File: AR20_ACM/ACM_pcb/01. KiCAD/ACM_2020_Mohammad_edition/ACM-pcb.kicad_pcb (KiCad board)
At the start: 2 copper layers, 19.9 x 28 mm, 32 parts, among them J1 TC2030-MCP-NL, P1 Conn_02x15_Odd_Even, Q1 Q_PMOS_DGS, U1 ATmega328P-AU, U2 MCP25625-x-SS, U3 NCV890430MW50TXG, Y1 16.0Mhz

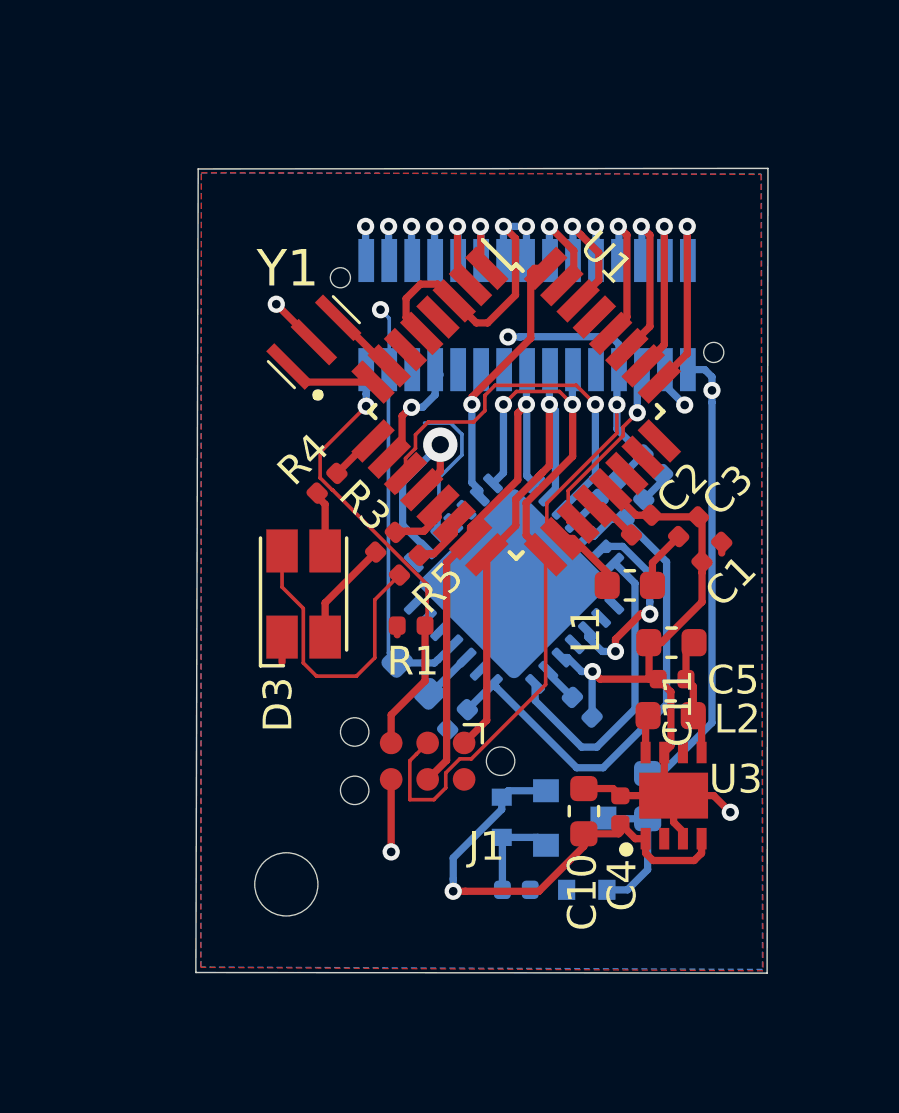
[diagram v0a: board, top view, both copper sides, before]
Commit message: ACM-pcb full connected
ACM -12.01
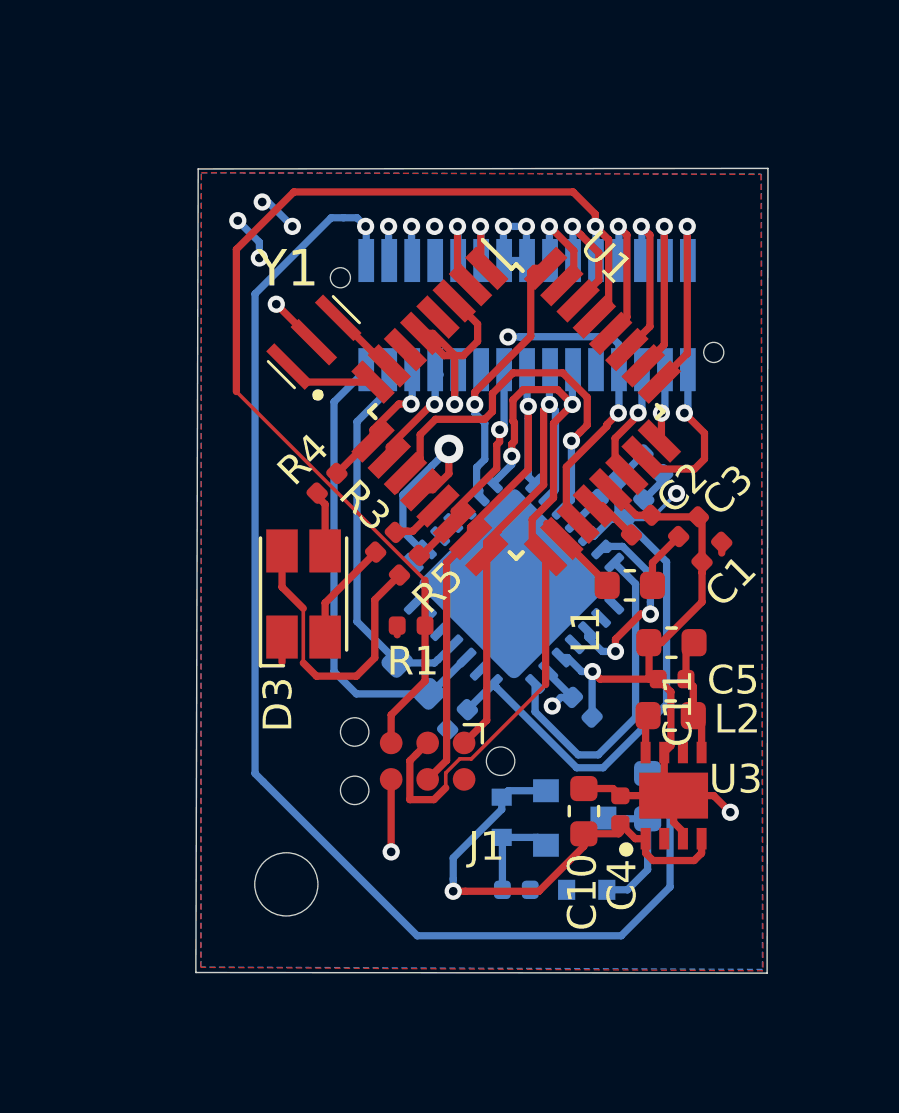
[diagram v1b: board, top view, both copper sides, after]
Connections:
- net /U-Pin19 renamed Net-(P1-Pad19)
- net /U-Pin9 renamed Net-(P1-Pad9)
- P1 pad 1: +12V -> /U-Pin1
- P1 pad 10: /U-Pin10 -> /Reset
- P1 pad 17: /U-Pin17 -> /BLUE_LED
- P1 pad 21: /U-Pin21 -> GND
- P1 pad 24: /U-Pin24 -> GND
- P1 pad 25: /U-Pin25 -> /GREEN_LED
- P1 pad 28: /U-Pin28 -> +5V
- P1 pad 29: /Reset -> /U-Pin29
- P1 pad 30: /U-Pin30 -> +12V
- P1 pad 7: +5V -> /U-Pin7
- R7 pad 2: /U-Pin1 -> /U-Pin29
- U1 pad 19: /U-Pin5 -> /U-Pin7
- U1 pad 22: Net-(U1-Pad22) -> /U-Pin5
- U1 pad 23: /U-Pin7 -> /U-Pin1
- U1 pad 24: Net-(U1-Pad24) -> /U-Pin3
- U2 pad 3: /U-Pin1 -> /U-Pin29
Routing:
- net +12V: track 16.0 -> 44.8 mm
- net /Reset: track 15.7 -> 39.2 mm
- net /U-Pin29: track 0.00 -> 16.5 mm
- net /U-Pin7: track 0.00 -> 11.3 mm, vias 0 -> 2
- net /BLUE_LED: track 1.96 -> 7.77 mm, vias 0 -> 1
- net GND: track 51.4 -> 45.6 mm, vias 6 -> 7
- net +5V: track 43.6 -> 38.6 mm, vias 2 -> 7
- net /U-Pin1: track 1.84 -> 5.93 mm, vias 0 -> 1
- net /GREEN_LED: track 1.81 -> 5.11 mm, vias 0 -> 1
- net /U-Pin5: track 6.72 -> 4.17 mm
- net /U-Pin3: track 1.55 -> 3.14 mm
- net /U-Pin27: track 14.8 -> 13.5 mm, vias 1 -> 0
- net /U-Pin30: track 1.20 -> 0.00 mm, vias 1 -> 0
- net /U-Pin28: track 1.20 -> 0.00 mm, vias 1 -> 0
- net /U-Pin10: track 1.20 -> 0.00 mm, vias 1 -> 0
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
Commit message: final one 12.01
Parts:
- moved C1 14.3 mm to (69.8, 68.3)
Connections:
- net Net-(P1-Pad9) renamed /U-Pin9
- P1 pad 19: Net-(P1-Pad19) -> GND
- P1 pad 24: GND -> +5V
- P1 pad 26: /U-Pin26 -> +5V
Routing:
- net +5V: track 38.6 -> 29.8 mm, vias 7 -> 13
- net /Reset: track 39.2 -> 45.4 mm
- net +12V_Safe: track 17.1 -> 13.6 mm
- net GND: track 45.6 -> 42.6 mm, vias 7 -> 12
- net Net-(D3-Pad2): track 10.4 -> 12.7 mm
- net /U-Pin9: track 0.03 -> 1.25 mm, vias 0 -> 1
- net /U-Pin26: track 1.20 -> 0.00 mm, vias 1 -> 0
- net +12V: track 44.8 -> 45.8 mm
- net (no net): vias 1 -> 0

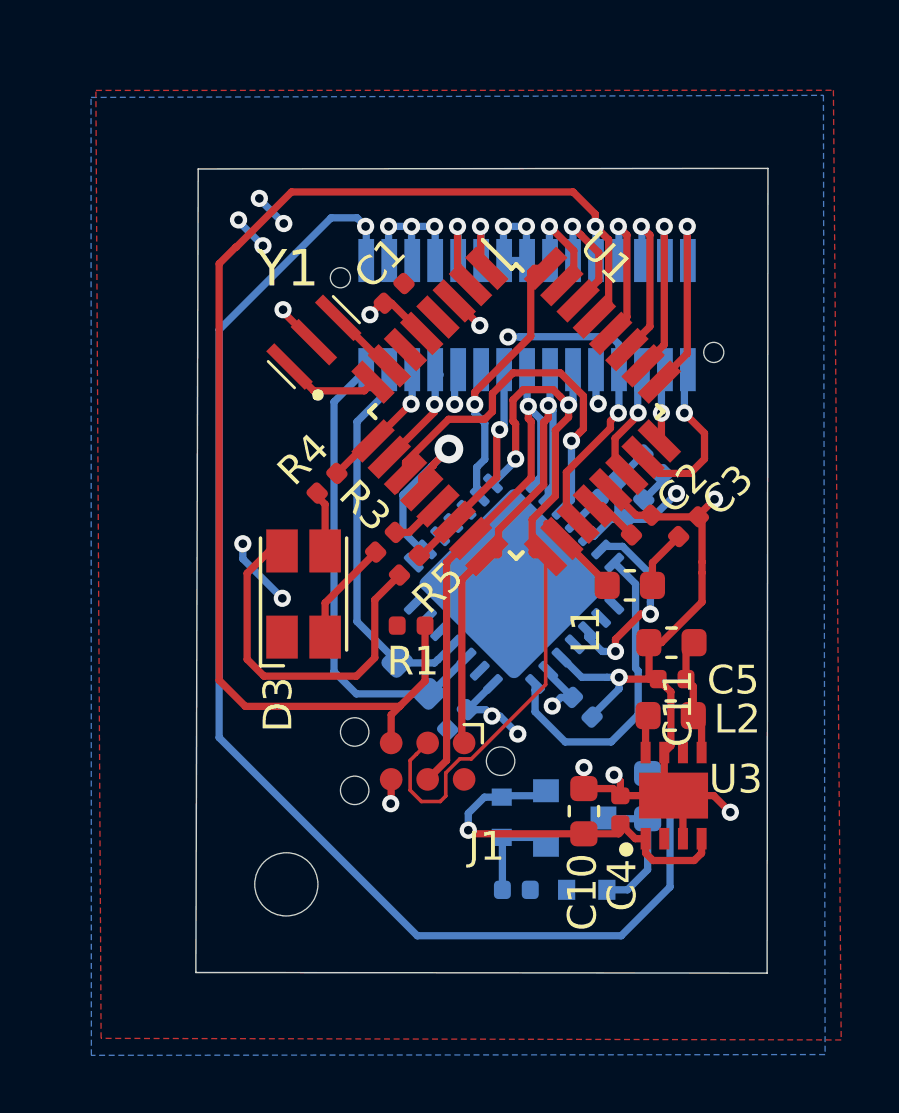
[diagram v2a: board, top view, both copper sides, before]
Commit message: Ronded corner and added a angle
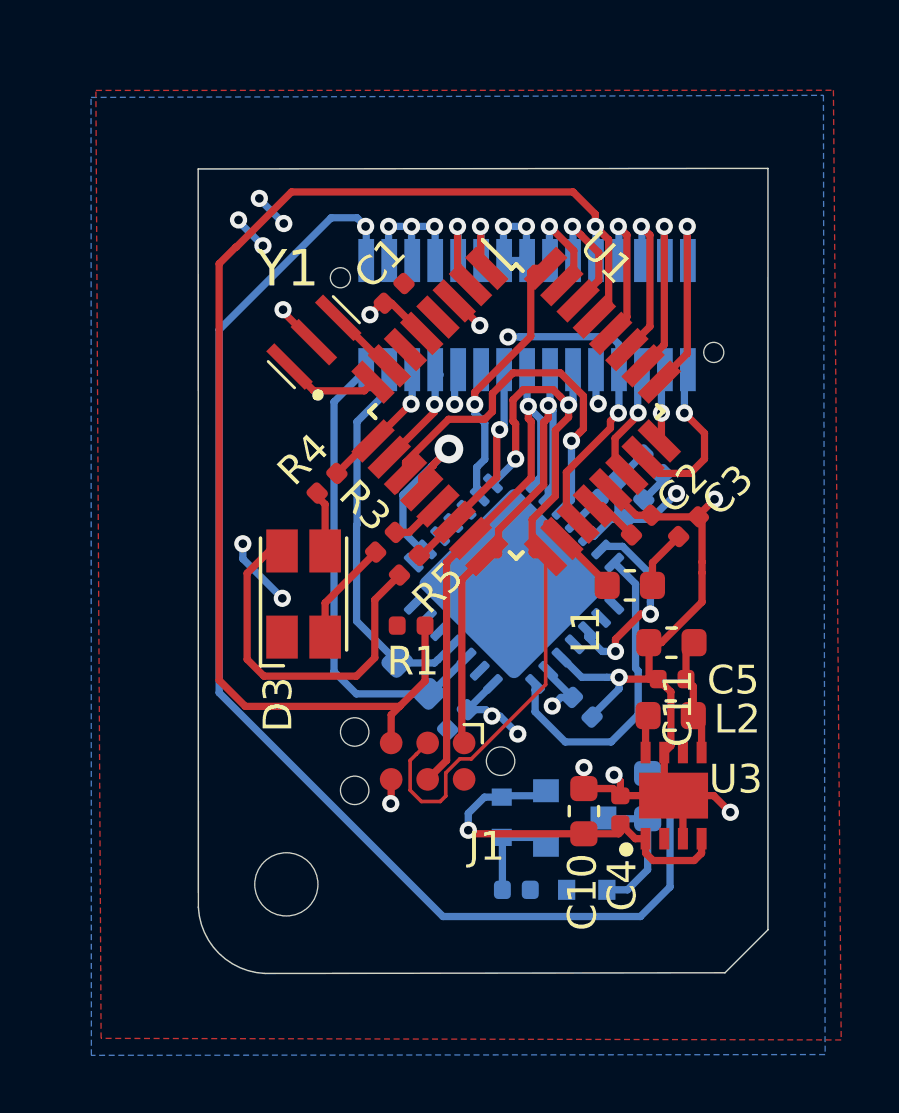
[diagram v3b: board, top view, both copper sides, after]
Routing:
- net +12V: track 45.8 -> 44.3 mm
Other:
- board size 19.9 x 28 mm -> 19.8 x 28 mm

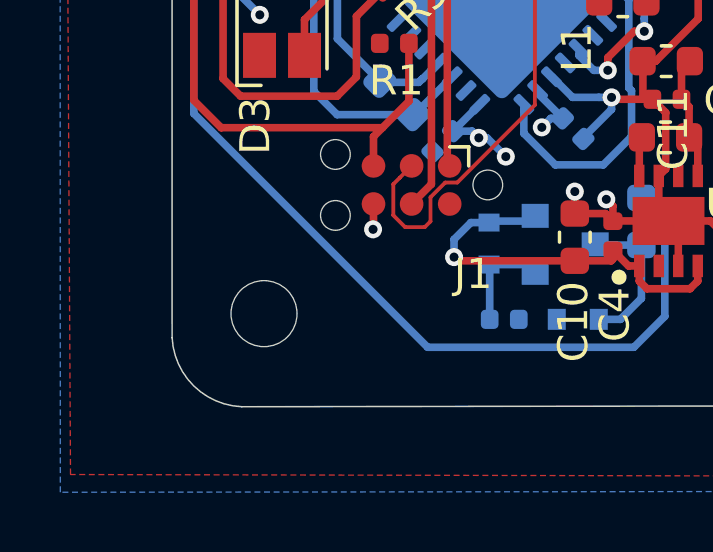
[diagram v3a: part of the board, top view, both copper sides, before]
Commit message: Set PCB Size and started on ACM footprint
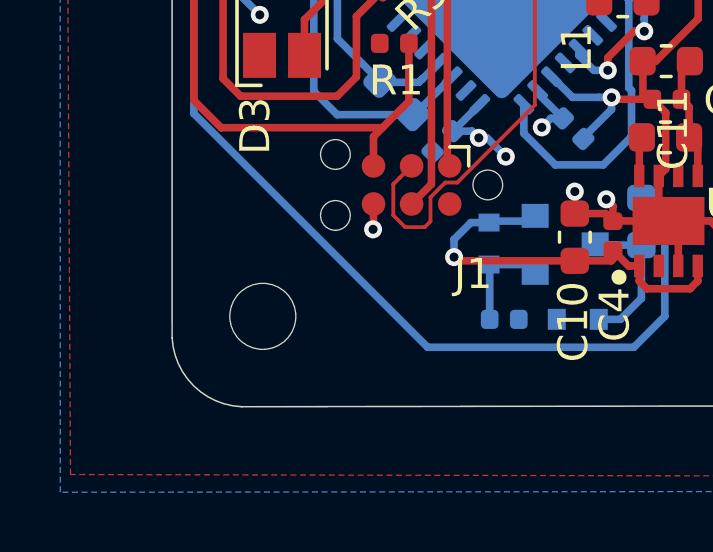
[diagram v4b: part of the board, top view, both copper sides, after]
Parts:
- moved H1 0.10 mm to (66.0, 89.0)
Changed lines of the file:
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@@
   )
   (module MountingHole:MountingHole_2.2mm_M2 (layer B.Cu)
-    (at 66.04 88.91)
+    (at 66 89)
     (descr "Mounting Hole 2.2mm, no annular, M2")
     (tags "mounting hole 2.2mm no annular m2")

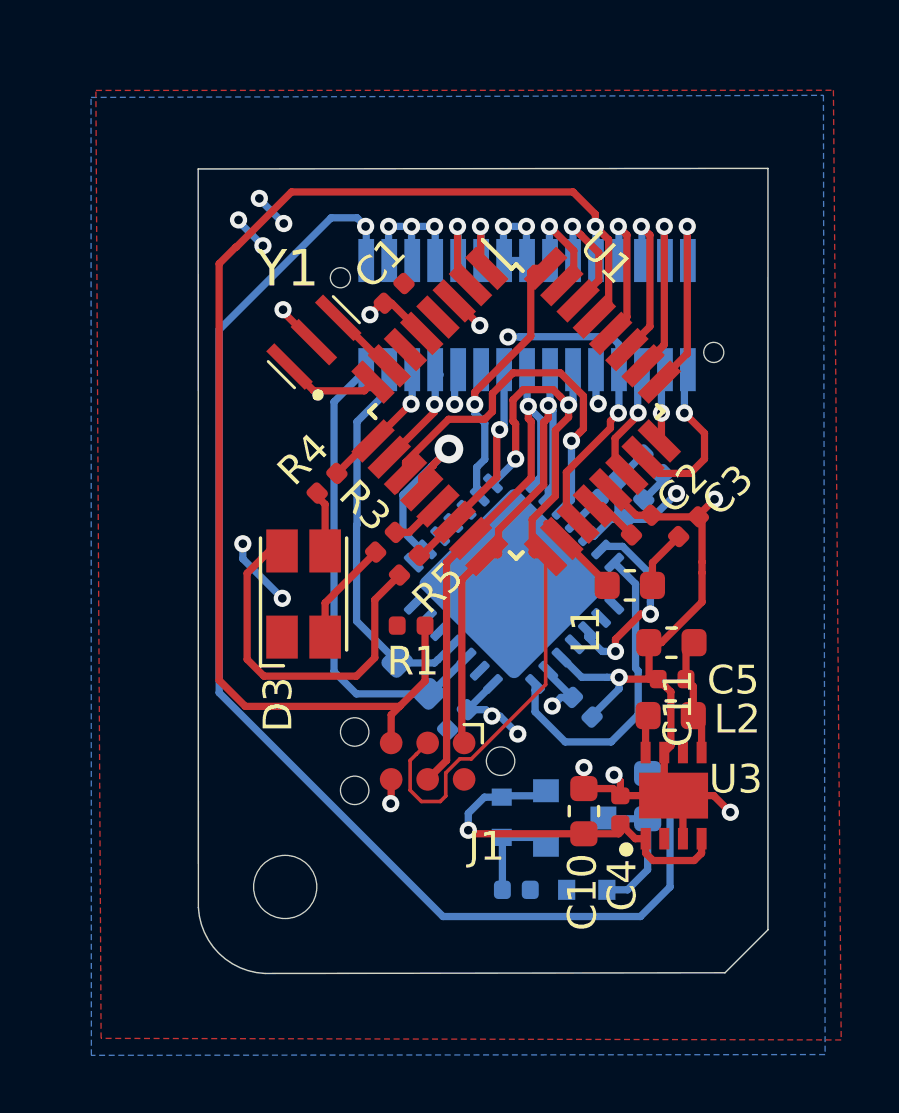
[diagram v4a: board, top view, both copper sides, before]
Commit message: Added GND to Pin 9 and checked connector output
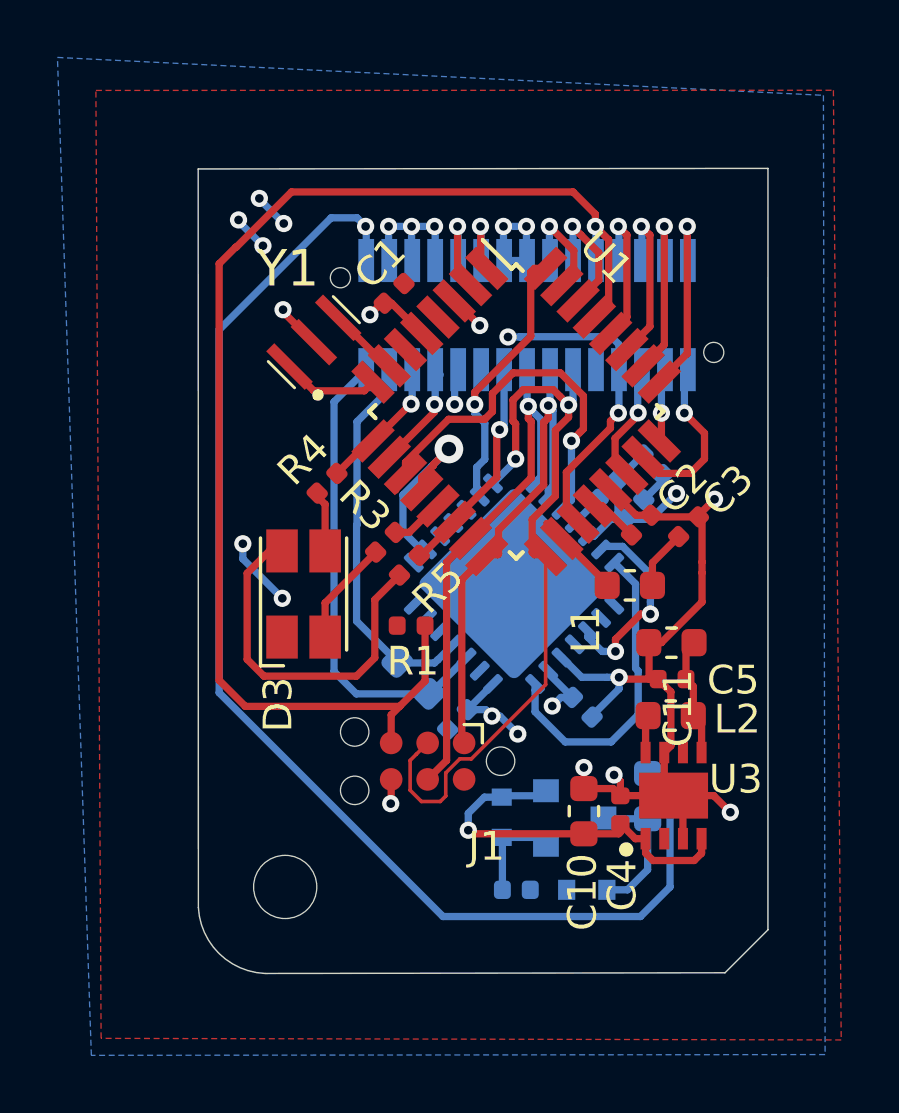
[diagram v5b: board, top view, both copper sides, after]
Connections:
- P1 pad 9: /U-Pin9 -> GND
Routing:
- net /U-Pin9: track 1.25 -> 0.00 mm, vias 1 -> 0
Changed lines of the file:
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@@
     (thickness 1)
     (drawings 9)
-    (tracks 491)
+    (tracks 488)
     (zones 0)
     (modules 32)
-    (nets 55)
+    (nets 54)
   )
   (page A4)
@@
   (net 52 /U-Pin27)
   (net 53 /U-Pin29)
-  (net 54 /U-Pin9)
   (net_class Default "This is the default net class."
     (clearance 0.0889)
@@
     (add_net /U-Pin7)
     (add_net /U-Pin8)
-    (add_net /U-Pin9)
     (add_net GND)
     (add_net "Net-(C2-Pad1)")
@@
       (net 26 /U-Pin8))
     (pad 9 smd rect (at -2.4 -1.9 180) (size 0.55 1.5) (layers B.Cu B.Paste B.Mask)
-      (net 54 /U-Pin9))
+      (net 2 GND))
     (pad 10 smd rect (at -2.4 1.9 180) (size 0.55 1.5) (layers B.Cu B.Paste B.Mask)
       (net 3 /Reset))
@@
   (segment (start 68.822 70.988) (end 67.7 72.11) (width 0.254) (layer B.Cu) (net 53))
   (segment (start 67.7 72.11) (end 67.7 81.5) (width 0.254) (layer B.Cu) (net 53))
-  (segment (start 76.8 71.01) (end 76.822 70.988) (width 0.254) (layer B.Cu) (net 54))
-  (via (at 76.9 72.175) (size 0.6) (drill 0.3) (layers F.Cu B.Cu) (net 54))
-  (segment (start 76.822 72.097) (end 76.9 72.175) (width 0.254) (layer B.Cu) (net 54))
-  (segment (start 76.822 70.988) (end 76.822 72.097) (width 0.254) (layer B.Cu) (net 54))
+  (segment (start 76.8 71.01) (end 76.822 70.988) (width 0.254) (layer B.Cu) (net 2))
   (zone (net 6) (net_name +5V) (layer F.Cu) (hatch edge 0.508)
     (connect_pads (clearance 0.127))
@@
     (polygon
       (pts
-        (xy 84.799525 94.8364) (xy 59.250475 94.8636) (xy 59.239763 61.5089) (xy 84.740713 61.4361)
+        (xy 84.799525 94.8364) (xy 59.250475 94.8636) (xy 58.06948 60.11672) (xy 84.740713 61.4361)
       )
     )
